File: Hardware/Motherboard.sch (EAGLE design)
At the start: 64 parts, among them J1 MICROMOD-2222-C, J10 MICRO-SD-PUSH-PUSH-EXT-PIN, J2 Vertical Qwiic Connector, J4 QWIIC_RIGHT_ANGLE, J5 CORTEX_JTAG_DEBUG_MINIMUM_PTH, J6 MICROMOD_CARRIER, J7 MICROMOD_CARRIER, U2 MCP73831, U5 AP7361C-33

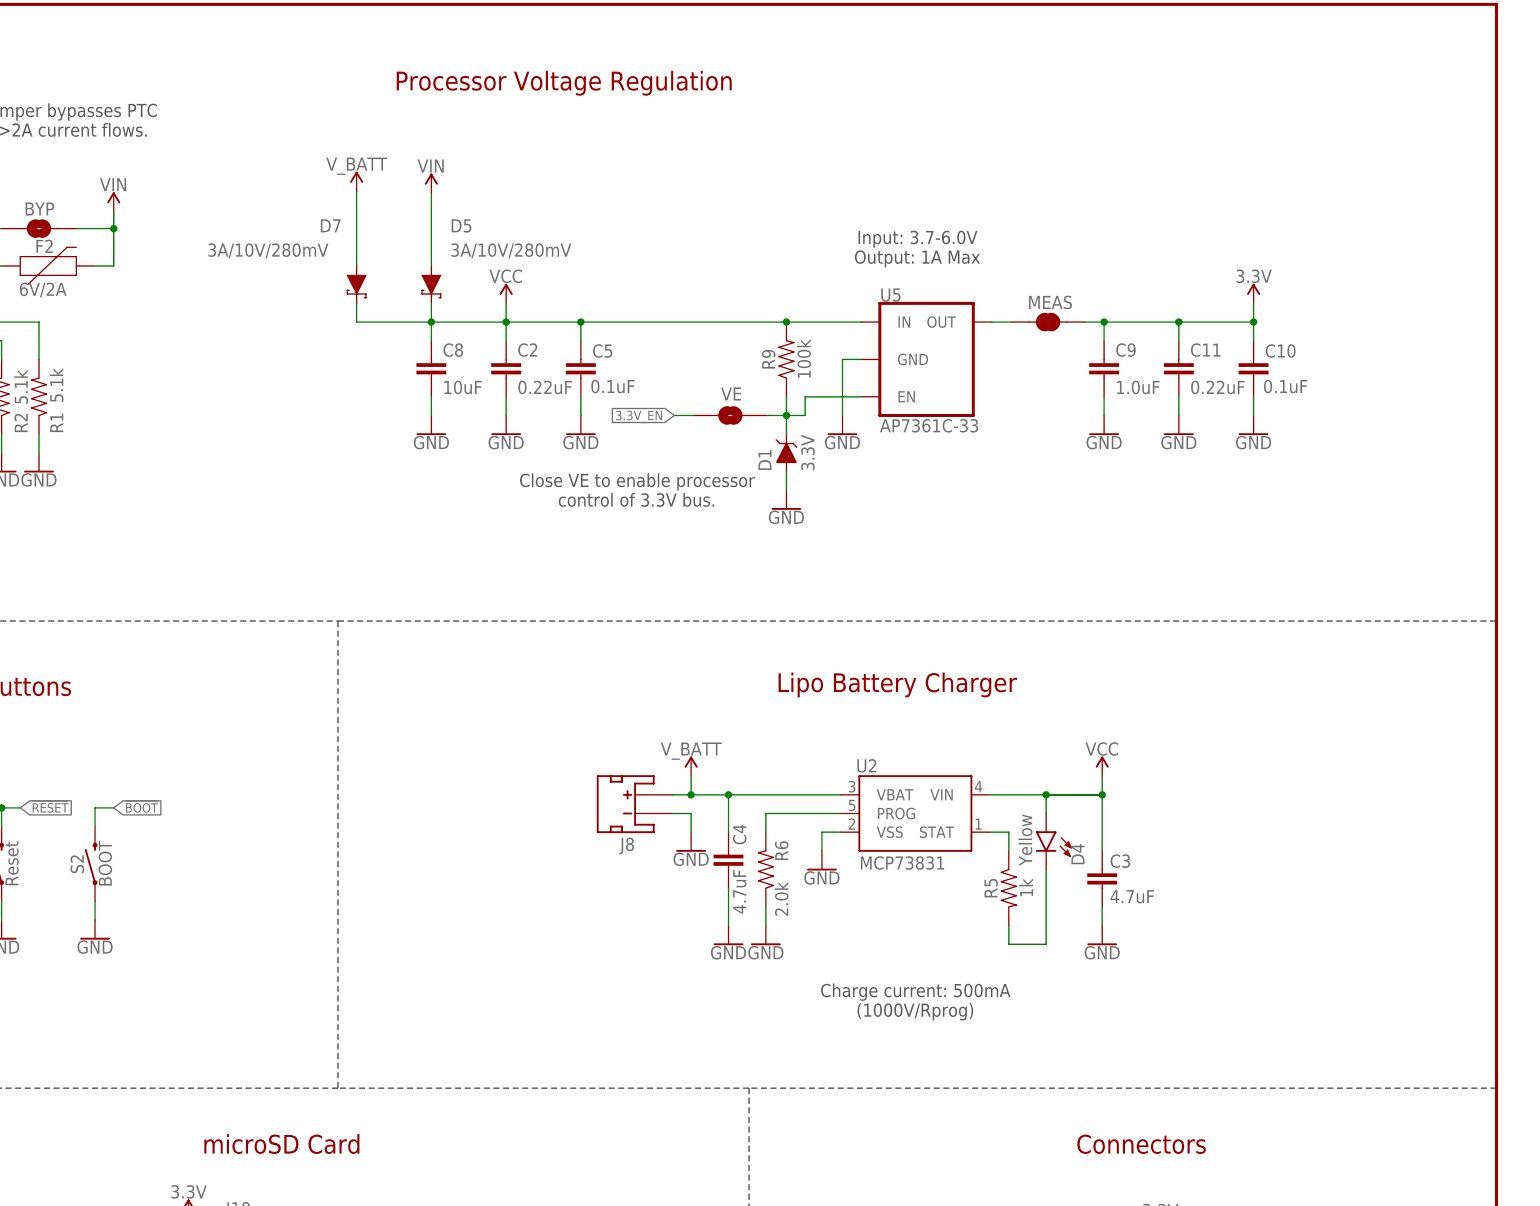
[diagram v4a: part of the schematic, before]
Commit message: Adds 2 pin dip switch for charge selection, switches diode to PCHN MOSFET to VBAT net
* Adds better silk
*  Adds charge selection table to schematic
* Moves standoffs around
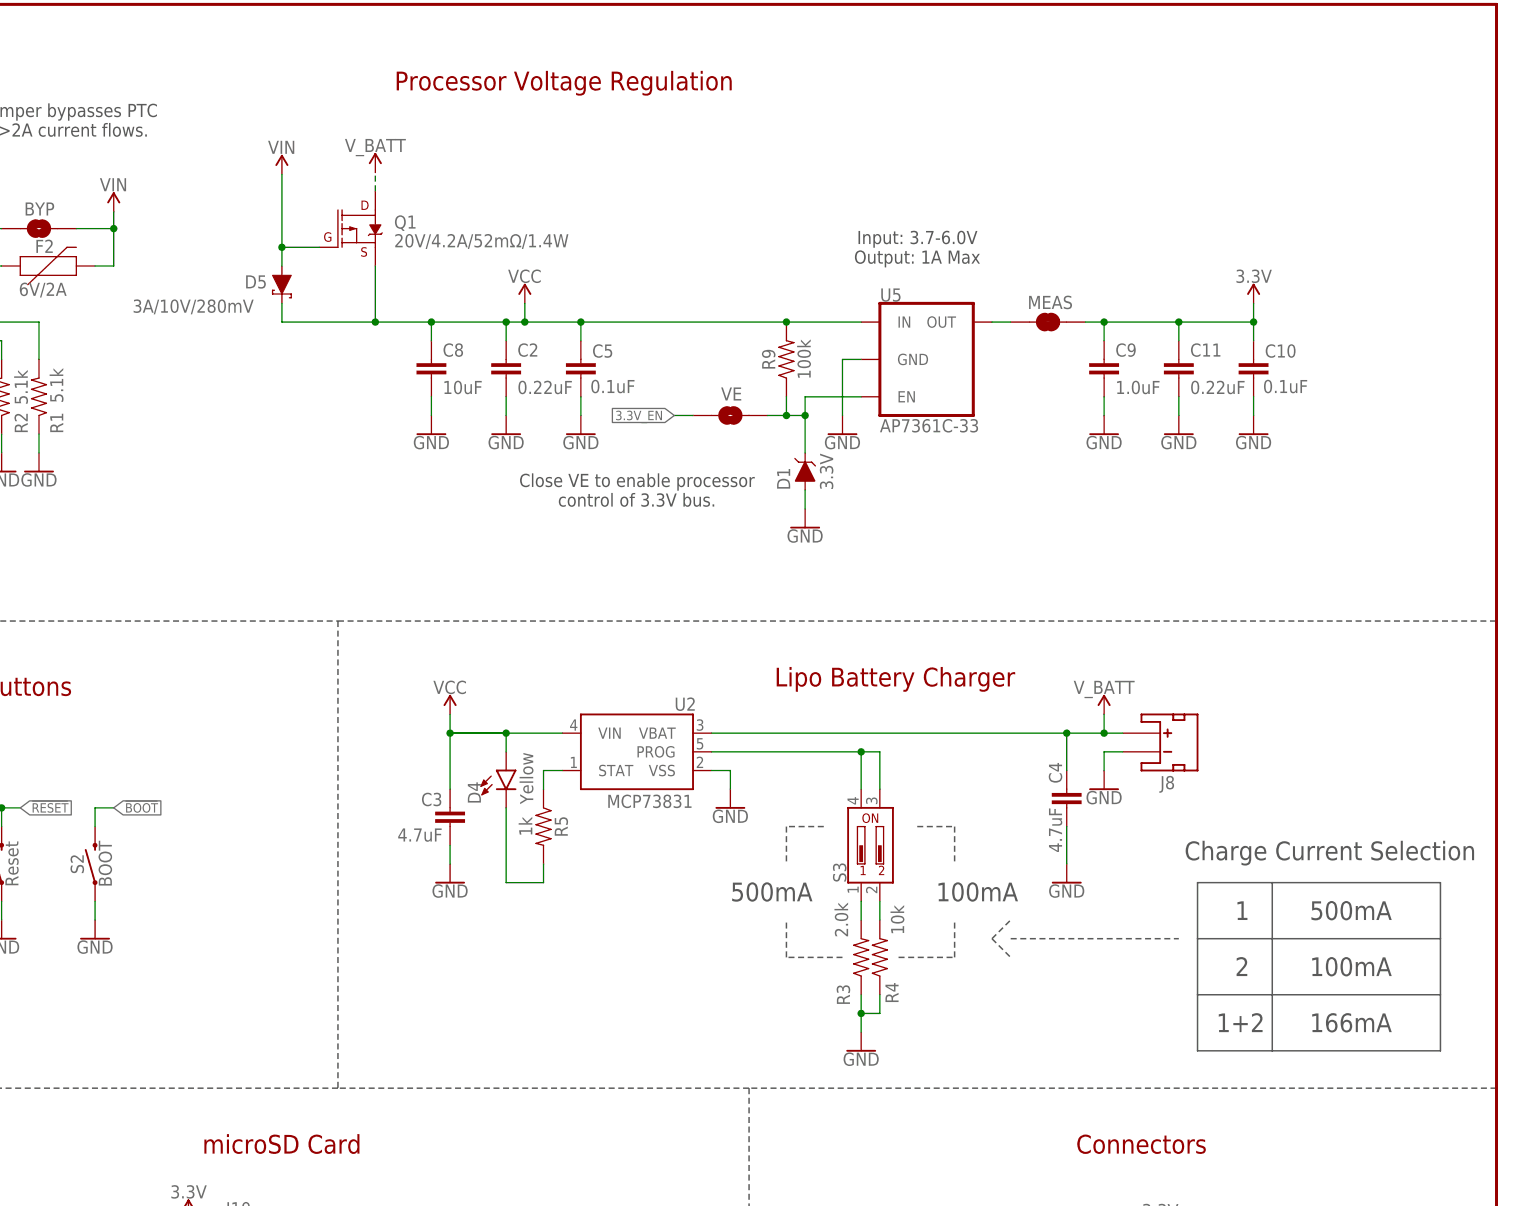
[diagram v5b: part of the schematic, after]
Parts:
- removed D7: 3A/10V/280mV, SparkFun-DiscreteSemi:DIODE-SCHOTTKY-BAT60A
- removed R6: 2.0k, SparkFun-Resistors:2.0KOHM-0603-1/10W-5%
- added Q1: 20V/4.2A/52mΩ/1.4W, SparkFun-DiscreteSemi:MOSFET_PCH-DMG2305UX-7
- added R3: 2.0k, SparkFun-Resistors:2.0KOHM-0603-1/10W-5%
- added R4: 10k, SparkFun-Resistors:10KOHM-0603-1/10W-1%
- added S3: DIP-02-SMD-50MIL, SparkFun-Switches:DIP-02-SMD-50MIL
- LOGO3: value OSHW-LOGOS -> OSHW-LOGOL; device SparkFun-Aesthetics:OSHW-LOGOS -> SparkFun-Aesthetics:OSHW-LOGOL
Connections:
- new net N$6: S3.P$3, S3.P$4, U2.PROG
- new net N$9: R4.2, S3.P$2
- net GND: now also R3.1, R4.1; no longer R6.1
- net N$8: now also R3.2, S3.P$1; no longer R6.2, U2.PROG
- net VCC: now also Q1.S; no longer D7.C
- net VIN: now also Q1.G
- net V_BATT: now also Q1.D; no longer D7.A
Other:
- note added: "1"
- note added: "1+2"
- note added: "100mA"
- note added: "166mA"
- note added: "2"
- note added: "500mA"
- note added: "Charge Current Selection"
- note removed: "Charge current: 500mA (1000V/Rprog)"
- moved on the sheet: C3, C4, D1, D4, D5, J8, R5, U2

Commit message: Moved something in the schematic
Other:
- note added: "Standoff"
- moved on the sheet: J5
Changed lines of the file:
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@@
 <part name="GND3" library="SparkFun-PowerSymbols" deviceset="GND" device=""/>
 <part name="Q1" library="SparkFun-DiscreteSemi" deviceset="MOSFET_PCH" device="-DMG2305UX-7" value="20V/4.2A/52mΩ/1.4W"/>
+<part name="GND6" library="SparkFun-PowerSymbols" deviceset="GND" device=""/>
 </parts>
 <sheets>
@@
 <wire x1="330.2" y1="76.2" x2="330.2" y2="35.56" width="0.2032" layer="97" style="longdash"/>
 <wire x1="205.74" y1="132.08" x2="187.96" y2="132.08" width="0.2032" layer="97" style="longdash"/>
-<wire x1="187.96" y1="132.08" x2="0" y2="132.08" width="0.2032" layer="97" style="longdash"/>
-<wire x1="187.96" y1="132.08" x2="187.96" y2="195.58" width="0.2032" layer="97" style="longdash"/>
+<wire x1="187.96" y1="132.08" x2="167.64" y2="132.08" width="0.2032" layer="97" style="longdash"/>
+<wire x1="167.64" y1="132.08" x2="0" y2="132.08" width="0.2032" layer="97" style="longdash"/>
+<wire x1="187.96" y1="132.08" x2="187.96" y2="160.02" width="0.2032" layer="97" style="longdash"/>
+<wire x1="187.96" y1="160.02" x2="187.96" y2="195.58" width="0.2032" layer="97" style="longdash"/>
 <wire x1="187.96" y1="195.58" x2="187.96" y2="279.4" width="0.2032" layer="97" style="longdash"/>
 <wire x1="187.96" y1="195.58" x2="274.32" y2="195.58" width="0.2032" layer="97" style="longdash"/>
@@
 <text x="406.4" y="139.7" size="2.54" layer="97" font="vector">166mA</text>
 <wire x1="365.76" y1="152.4" x2="388.62" y2="152.4" width="0.2032" layer="97" style="dashdot"/>
+<wire x1="182.88" y1="0" x2="182.88" y2="27.94" width="0.2032" layer="97" style="longdash"/>
+<wire x1="182.88" y1="27.94" x2="205.74" y2="27.94" width="0.2032" layer="97" style="longdash"/>
+<wire x1="167.64" y1="132.08" x2="167.64" y2="160.02" width="0.2032" layer="97" style="longdash"/>
+<wire x1="167.64" y1="160.02" x2="187.96" y2="160.02" width="0.2032" layer="97" style="longdash"/>
+<text x="171.958" y="153.416" size="2.54" layer="94" font="vector">Standoff</text>
+<text x="187.96" y="22.86" size="2.54" layer="94" font="vector">Standoff</text>
 </plain>
 <instances>
@@
 <attribute name="REV" x="419.1" y="6.604" size="2.7432" layer="94" font="vector"/>
 </instance>
-<instance part="H3" gate="G$1" x="416.56" y="73.66" smashed="yes"/>
-<instance part="H8" gate="G$1" x="414.02" y="73.66" smashed="yes"/>
+<instance part="H3" gate="G$1" x="190.5" y="17.78" smashed="yes"/>
+<instance part="H8" gate="G$1" x="177.8" y="147.32" smashed="yes"/>
 <instance part="H14" gate="G$1" x="414.02" y="33.02" smashed="yes"/>
 <instance part="H15" gate="G$1" x="411.48" y="33.02" smashed="yes"/>
@@
 <attribute name="VALUE" x="254" y="86.106" size="1.778" layer="96" font="vector" align="top-center"/>
 </instance>
-<instance part="J5" gate="G$1" x="158.496" y="148.59" smashed="yes">
-<attribute name="NAME" x="148.336" y="156.464" size="1.778" layer="95" font="vector"/>
-</instance>
-<instance part="GND14" gate="1" x="143.256" y="140.97" smashed="yes">
-<attribute name="VALUE" x="143.256" y="140.716" size="1.778" layer="96" font="vector" align="top-center"/>
-</instance>
-<instance part="SUPPLY10" gate="G$1" x="143.256" y="156.21" smashed="yes">
-<attribute name="VALUE" x="143.256" y="159.004" size="1.778" layer="96" font="vector" align="bottom-center"/>
+<instance part="J5" gate="G$1" x="158.496" y="255.27" smashed="yes">
+<attribute name="NAME" x="148.336" y="263.144" size="1.778" layer="95" font="vector"/>
+</instance>
+<instance part="GND14" gate="1" x="143.256" y="247.65" smashed="yes">
+<attribute name="VALUE" x="143.256" y="247.396" size="1.778" layer="96" font="vector" align="top-center"/>
+</instance>
+<instance part="SUPPLY10" gate="G$1" x="143.256" y="262.89" smashed="yes">
+<attribute name="VALUE" x="143.256" y="265.684" size="1.778" layer="96" font="vector" align="bottom-center"/>
 </instance>
 <instance part="FD1" gate="G$1" x="393.7" y="33.02" smashed="yes"/>
@@
 <attribute name="VALUE" x="281.94" y="93.726" size="1.778" layer="96" font="vector" align="top-center"/>
 </instance>
-<instance part="H2" gate="G$1" x="419.1" y="73.66" smashed="yes"/>
-<instance part="H4" gate="G$1" x="421.64" y="73.66" smashed="yes"/>
-<instance part="GND40" gate="1" x="421.64" y="63.5" smashed="yes">
-<attribute name="VALUE" x="421.64" y="63.246" size="1.778" layer="96" font="vector" align="top-center"/>
+<instance part="H2" gate="G$1" x="193.04" y="17.78" smashed="yes"/>
+<instance part="H4" gate="G$1" x="195.58" y="17.78" smashed="yes"/>
+<instance part="GND40" gate="1" x="195.58" y="7.62" smashed="yes">
+<attribute name="VALUE" x="195.58" y="7.366" size="1.778" layer="96" font="vector" align="top-center"/>
 </instance>
 <instance part="SUPPLY9" gate="G$1" x="24.638" y="91.186" smashed="yes">
@@
 <attribute name="NAME" x="281.94" y="248.92" size="1.778" layer="95" font="vector"/>
 <attribute name="VALUE" x="281.94" y="246.38" size="1.778" layer="96" font="vector"/>
+</instance>
+<instance part="GND6" gate="1" x="177.8" y="139.7" smashed="yes">
+<attribute name="VALUE" x="177.8" y="139.446" size="1.778" layer="96" font="vector" align="top-center"/>
 </instance>
 </instances>
@@
 <segment>
 <pinref part="J5" gate="G$1" pin="VCC"/>
-<wire x1="145.796" y1="153.67" x2="143.256" y2="153.67" width="0.1524" layer="91"/>
-<wire x1="143.256" y1="153.67" x2="143.256" y2="156.21" width="0.1524" layer="91"/>
+<wire x1="145.796" y1="260.35" x2="143.256" y2="260.35" width="0.1524" layer="91"/>
+<wire x1="143.256" y1="260.35" x2="143.256" y2="262.89" width="0.1524" layer="91"/>
 <pinref part="SUPPLY10" gate="G$1" pin="3.3V"/>
 </segment>
@@
 <segment>
 <pinref part="J5" gate="G$1" pin="GND"/>
-<wire x1="145.796" y1="146.05" x2="143.256" y2="146.05" width="0.1524" layer="91"/>
+<wire x1="145.796" y1="252.73" x2="143.256" y2="252.73" width="0.1524" layer="91"/>
 <pinref part="GND14" gate="1" pin="GND"/>
-<wire x1="143.256" y1="146.05" x2="143.256" y2="143.51" width="0.1524" layer="91"/>
+<wire x1="143.256" y1="252.73" x2="143.256" y2="250.19" width="0.1524" layer="91"/>
 </segment>
 <segment>
@@
 </segment>
 <segment>
+<pinref part="GND6" gate="1" pin="GND"/>
 <pinref part="H8" gate="G$1" pin="1"/>
-<wire x1="414.02" y1="71.12" x2="414.02" y2="68.58" width="0.1524" layer="91"/>
-<wire x1="414.02" y1="68.58" x2="416.56" y2="68.58" width="0.1524" layer="91"/>
-<wire x1="416.56" y1="68.58" x2="419.1" y2="68.58" width="0.1524" layer="91"/>
-<wire x1="419.1" y1="68.58" x2="421.64" y2="68.58" width="0.1524" layer="91"/>
+<wire x1="177.8" y1="144.78" x2="177.8" y2="142.24" width="0.1524" layer="91"/>
+</segment>
+<segment>
+<wire x1="190.5" y1="12.7" x2="193.04" y2="12.7" width="0.1524" layer="91"/>
+<wire x1="193.04" y1="12.7" x2="195.58" y2="12.7" width="0.1524" layer="91"/>
 <pinref part="GND40" gate="1" pin="GND"/>
-<wire x1="421.64" y1="66.04" x2="421.64" y2="68.58" width="0.1524" layer="91"/>
-<junction x="421.64" y="68.58"/>
+<wire x1="195.58" y1="10.16" x2="195.58" y2="12.7" width="0.1524" layer="91"/>
+<junction x="195.58" y="12.7"/>
 <pinref part="H4" gate="G$1" pin="1"/>
-<wire x1="421.64" y1="71.12" x2="421.64" y2="68.58" width="0.1524" layer="91"/>
+<wire x1="195.58" y1="15.24" x2="195.58" y2="12.7" width="0.1524" layer="91"/>
 <pinref part="H2" gate="G$1" pin="1"/>
-<wire x1="419.1" y1="71.12" x2="419.1" y2="68.58" width="0.1524" layer="91"/>
-<junction x="419.1" y="68.58"/>
+<wire x1="193.04" y1="15.24" x2="193.04" y2="12.7" width="0.1524" layer="91"/>
+<junction x="193.04" y="12.7"/>
 <pinref part="H3" gate="G$1" pin="1"/>
-<wire x1="416.56" y1="71.12" x2="416.56" y2="68.58" width="0.1524" layer="91"/>
-<junction x="416.56" y="68.58"/>
+<wire x1="190.5" y1="15.24" x2="190.5" y2="12.7" width="0.1524" layer="91"/>
 </segment>
 <segment>
@@
 <segment>
 <pinref part="J5" gate="G$1" pin="!RESET"/>
-<wire x1="168.656" y1="153.67" x2="171.196" y2="153.67" width="0.1524" layer="91"/>
-<label x="171.196" y="153.67" size="1.27" layer="95" font="vector" xref="yes"/>
+<wire x1="168.656" y1="260.35" x2="171.196" y2="260.35" width="0.1524" layer="91"/>
+<label x="171.196" y="260.35" size="1.27" layer="95" font="vector" xref="yes"/>
 </segment>
 <segment>
@@
 <segment>
 <pinref part="J5" gate="G$1" pin="SWDIO"/>
-<wire x1="168.656" y1="151.13" x2="171.196" y2="151.13" width="0.1524" layer="91"/>
-<label x="171.196" y="151.13" size="1.27" layer="95" font="vector" xref="yes"/>
+<wire x1="168.656" y1="257.81" x2="171.196" y2="257.81" width="0.1524" layer="91"/>
+<label x="171.196" y="257.81" size="1.27" layer="95" font="vector" xref="yes"/>
 </segment>
 <segment>
@@
 <segment>
 <pinref part="J5" gate="G$1" pin="SWDCLK"/>
-<wire x1="168.656" y1="148.59" x2="171.196" y2="148.59" width="0.1524" layer="91"/>
-<label x="171.196" y="148.59" size="1.27" layer="95" font="vector" xref="yes"/>
-</segment>
-</net>
+<wire x1="168.656" y1="255.27" x2="171.196" y2="255.27" width="0.1524" layer="91"/>
+<label x="171.196" y="255.27" size="1.27" layer="95" font="vector" xref="yes"/>
+</segment>
+</net>

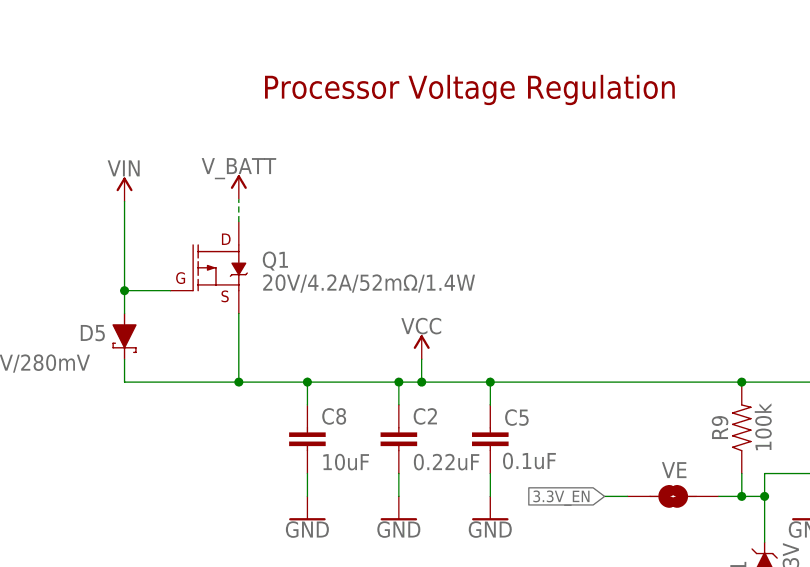
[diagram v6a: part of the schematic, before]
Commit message: Replace MOSFET with another one
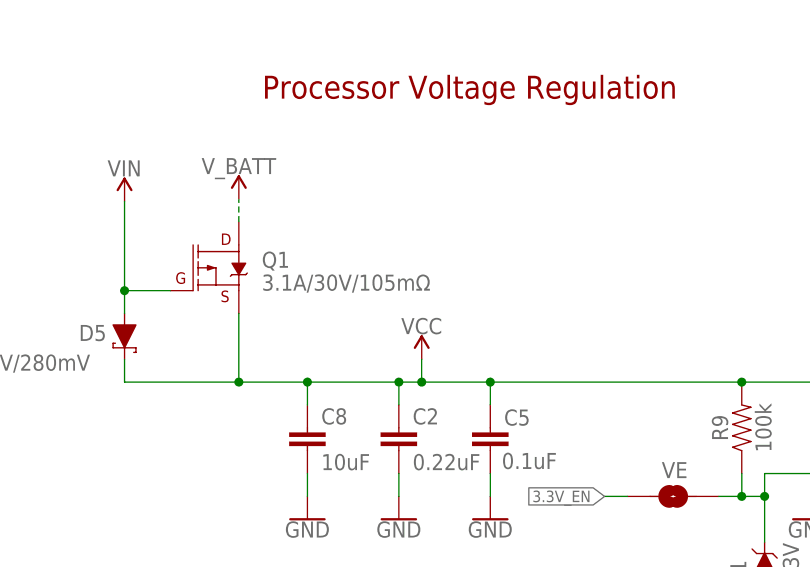
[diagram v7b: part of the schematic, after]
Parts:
- Q1: value 20V/4.2A/52mΩ/1.4W -> 3.1A/30V/105mΩ; device SparkFun-DiscreteSemi:MOSFET_PCH-DMG2305UX-7 -> SparkFun-DiscreteSemi:MOSFET_PCH-DMG2307L
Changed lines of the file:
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@@
 <part name="R4" library="SparkFun-Resistors" deviceset="10KOHM" device="-0603-1/10W-1%" value="10k"/>
 <part name="GND3" library="SparkFun-PowerSymbols" deviceset="GND" device=""/>
-<part name="Q1" library="SparkFun-DiscreteSemi" deviceset="MOSFET_PCH" device="-DMG2305UX-7" value="20V/4.2A/52mΩ/1.4W"/>
+<part name="Q1" library="SparkFun-DiscreteSemi" deviceset="MOSFET_PCH" device="-DMG2307L" value="3.1A/30V/105mΩ"/>
 <part name="GND6" library="SparkFun-PowerSymbols" deviceset="GND" device=""/>
 </parts>
